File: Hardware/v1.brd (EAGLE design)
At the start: 50 x 40 mm, 82 parts, among them IC1 LM324D, IC2 m328p, IC3 REG1117, J1 22-27-2061-06, J2 22-27-2021-02, J3 22-27-2021-02, J4 22-27-2031-03, J5 22-27-2041-04, Q1 BSS123, Q2 BSS123, Q3 BSS123, Q5 BSS123

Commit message: solved all from #17
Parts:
- added R30: 1k, rcl:R0603
- moved TP4 5.48 mm to (27.4, 38.3), flipped to the bottom
- moved TP9 4.83 mm to (32.9, 38.4)
- moved TP10 4.65 mm to (33.3, 34.4)
- flipped TP6 to the top
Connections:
- new net N$27: C1.1, IC1.3, R30.2, TP4.TP
- net SENSOR0: now also R30.1; no longer C1.1, IC1.3, TP4.TP
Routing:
- net SENSOR0: track 63.8 -> 49.9 mm, vias 2 -> 1
- net N$27: track 0.00 -> 12.5 mm, vias 0 -> 1
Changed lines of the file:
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@@
 <?xml version="1.0" encoding="utf-8"?>
 <!DOCTYPE eagle SYSTEM "eagle.dtd">
-<eagle version="7.2.0">
+<eagle version="6.6.0">
 <drawing>
 <settings>
@@
 <layer number="32" name="bCream" color="7" fill="5" visible="no" active="yes"/>
 <layer number="33" name="tFinish" color="6" fill="3" visible="yes" active="yes"/>
-<layer number="34" name="bFinish" color="6" fill="6" visible="no" active="yes"/>
+<layer number="34" name="bFinish" color="6" fill="6" visible="yes" active="yes"/>
 <layer number="35" name="tGlue" color="7" fill="4" visible="no" active="yes"/>
 <layer number="36" name="bGlue" color="7" fill="5" visible="no" active="yes"/>
@@
 <text x="38.89375" y="39.0525" size="1.27" layer="33" font="vector" ratio="15" align="center">PD6</text>
 <text x="41.513125" y="33.9725" size="1.27" layer="33" font="vector" ratio="15" align="center">PD7</text>
-<text x="29.225875" y="37.7825" size="1.27" layer="33" font="vector" ratio="15" align="center">SENS0</text>
+<text x="31.670625" y="36.449" size="1.27" layer="34" font="vector" ratio="15" rot="MR0" align="center">SENS0</text>
 <text x="26.819225" y="9.877425" size="1.27" layer="33" font="vector" ratio="15" align="center">LK_0</text>
 <text x="14.6685" y="2.0955" size="1.27" layer="34" font="vector" ratio="15" rot="MR0" align="center">H</text>
@@
 <pass name="Default">
 <param name="RoutingGrid" value="3.125mil"/>
-<param name="AutoGrid" value="1"/>
-<param name="Efforts" value="0"/>
-<param name="TopRouterVariant" value="1"/>
 <param name="tpViaShape" value="round"/>
 <param name="PrefDir.1" value="|"/>
@@
 <attribute name="VALUE" x="30.11805" y="21.929725" size="0.0254" layer="28" rot="MR0"/>
 </element>
-<element name="TP4" library="testpad" package="B1,27" value="PTR1B1,27" x="32.8295" y="37.766625" smashed="yes">
-<attribute name="TP_SIGNAL_NAME" value="" x="32.1945" y="35.861625" size="1" layer="37"/>
-<attribute name="VALUE" x="32.1945" y="37.004625" size="0.0254" layer="27"/>
+<element name="TP4" library="testpad" package="B1,27" value="PTR1B1,27" x="27.3685" y="38.274625" smashed="yes" rot="MR0">
+<attribute name="TP_SIGNAL_NAME" value="" x="28.0035" y="36.369625" size="1" layer="38" rot="MR0"/>
+<attribute name="VALUE" x="28.0035" y="37.512625" size="0.0254" layer="28" rot="MR0"/>
 </element>
 <element name="TP5" library="testpad" package="B1,27" value="PTR1B1,27" x="28.622625" y="8.239125" smashed="yes">
@@
 <attribute name="NAME" x="34.3804" y="35.2791" size="1.143" layer="34" font="vector" ratio="15" rot="MR270"/>
 </element>
-<element name="TP6" library="testpad" package="B1,27" value="PTR1B1,27" x="2.159" y="25.908" smashed="yes" rot="MR0">
-<attribute name="TP_SIGNAL_NAME" value="" x="2.794" y="24.003" size="1" layer="38" rot="MR0"/>
-<attribute name="VALUE" x="2.794" y="25.146" size="0.0254" layer="28" rot="MR0"/>
+<element name="TP6" library="testpad" package="B1,27" value="PTR1B1,27" x="2.159" y="25.908" smashed="yes">
+<attribute name="TP_SIGNAL_NAME" value="" x="1.524" y="24.003" size="1" layer="37"/>
+<attribute name="VALUE" x="1.524" y="25.146" size="0.0254" layer="27"/>
 </element>
 <element name="TP8" library="testpad" package="B1,27" value="PTR1B1,27" x="9.0805" y="37.846" smashed="yes" rot="MR0">
@@
 <attribute name="VALUE" x="9.7155" y="37.084" size="0.0254" layer="28" rot="MR0"/>
 </element>
-<element name="TP9" library="testpad" package="B1,27" value="PTR1B1,27" x="28.067" y="38.227" smashed="yes" rot="MR0">
-<attribute name="TP_SIGNAL_NAME" value="" x="28.702" y="36.322" size="1" layer="38" rot="MR0"/>
-<attribute name="VALUE" x="28.702" y="37.465" size="0.0254" layer="28" rot="MR0"/>
-</element>
-<element name="TP10" library="testpad" package="B1,27" value="PTR1B1,27" x="30.6705" y="38.1635" smashed="yes" rot="MR0">
-<attribute name="TP_SIGNAL_NAME" value="" x="31.3055" y="36.2585" size="1" layer="38" rot="MR0"/>
-<attribute name="VALUE" x="31.3055" y="37.4015" size="0.0254" layer="28" rot="MR0"/>
+<element name="TP9" library="testpad" package="B1,27" value="PTR1B1,27" x="32.893" y="38.354" smashed="yes" rot="MR0">
+<attribute name="TP_SIGNAL_NAME" value="" x="33.528" y="36.449" size="1" layer="38" rot="MR0"/>
+<attribute name="VALUE" x="33.528" y="37.592" size="0.0254" layer="28" rot="MR0"/>
+</element>
+<element name="TP10" library="testpad" package="B1,27" value="PTR1B1,27" x="33.3375" y="34.3535" smashed="yes" rot="MR0">
+<attribute name="TP_SIGNAL_NAME" value="" x="33.9725" y="32.4485" size="1" layer="38" rot="MR0"/>
+<attribute name="VALUE" x="33.9725" y="33.5915" size="0.0254" layer="28" rot="MR0"/>
 </element>
 <element name="C9" library="rcl" package="E5-13" value="1000u" x="30.5435" y="12.0015" smashed="yes" rot="MR90">
@@
 <element name="R29" library="rcl" package="R0603" value="280" x="17.78" y="16.7005" smashed="yes">
 <attribute name="NAME" x="16.1925" y="14.859" size="1.143" layer="33" font="vector" ratio="15" rot="R90"/>
+</element>
+<element name="R30" library="rcl" package="R0603" value="1k" x="30.4165" y="36.3855" smashed="yes" rot="R180">
+<attribute name="NAME" x="31.9405" y="38.481" size="1.27" layer="33" font="vector" ratio="15" rot="R180"/>
 </element>
 </elements>
@@
 <via x="15.1765" y="31.6865" extent="1-16" drill="0.4"/>
 <via x="15.5321" y="25.746075" extent="1-16" drill="0.4"/>
-<via x="29.4386" y="37.239575" extent="1-16" drill="0.4"/>
+<via x="29.3751" y="39.144575" extent="1-16" drill="0.4"/>
 <via x="32.4231" y="39.271575" extent="1-16" drill="0.4"/>
 <via x="9.8171" y="36.731575" extent="1-16" drill="0.4"/>
@@
 </signal>
 <signal name="SENSOR0">
-<via x="32.8295" y="36.03625" extent="1-16" drill="0.6"/>
-<contactref element="IC1" pad="3"/>
-<contactref element="C1" pad="1"/>
-<contactref element="TP4" pad="TP"/>
-<wire x1="32.8295" y1="37.766625" x2="32.8295" y2="36.03625" width="1" layer="1"/>
-<wire x1="32.8295" y1="36.03625" x2="35.94735" y2="32.9184" width="1" layer="1"/>
+<wire x1="32.48025" y1="36.3855" x2="35.94735" y2="32.9184" width="1" layer="1"/>
 <wire x1="35.94735" y1="32.9184" x2="41.8084" y2="32.9184" width="1" layer="1"/>
 <wire x1="41.8084" y1="32.9184" x2="43.894375" y2="30.832425" width="1" layer="1"/>
@@
 <wire x1="40.513" y1="3.683" x2="39.76034375" y2="3.683" width="1" layer="16"/>
 <wire x1="39.76034375" y1="3.683" x2="38.263425" y2="5.179921875" width="1" layer="16"/>
-<wire x1="21.62175" y1="32.658375" x2="21.62175" y2="34.89325" width="1" layer="16"/>
-<wire x1="21.62175" y1="34.89325" x2="22.819625" y2="36.091125" width="1" layer="16"/>
-<wire x1="22.819625" y1="36.091125" x2="25.49525" y2="36.091125" width="1" layer="16"/>
-<wire x1="25.49525" y1="36.091125" x2="32.774625" y2="36.091125" width="1" layer="16"/>
-<wire x1="32.774625" y1="36.091125" x2="32.8295" y2="36.03625" width="1" layer="16"/>
+<contactref element="R30" pad="1"/>
+<wire x1="32.48025" y1="36.3855" x2="31.2665" y2="36.3855" width="1" layer="1"/>
 </signal>
 <signal name="ENABLE_LED_1">
@@
 <wire x1="19.905" y1="16.7005" x2="18.63" y2="16.7005" width="0.254" layer="1"/>
 </signal>
+<signal name="N$27">
+<contactref element="TP4" pad="TP"/>
+<contactref element="IC1" pad="3"/>
+<contactref element="C1" pad="1"/>
+<contactref element="R30" pad="2"/>
+<wire x1="29.5665" y1="36.3855" x2="27.3685" y2="36.3855" width="1" layer="1"/>
+<via x="27.3685" y="36.3855" extent="1-16" drill="0.6"/>
+<wire x1="27.3685" y1="36.3855" x2="27.074125" y2="36.091125" width="1" layer="16"/>
+<wire x1="27.074125" y1="36.091125" x2="25.49525" y2="36.091125" width="1" layer="16"/>
+<wire x1="25.49525" y1="36.091125" x2="23.137125" y2="36.091125" width="1" layer="16"/>
+<wire x1="23.137125" y1="36.091125" x2="21.62175" y2="34.57575" width="1" layer="16"/>
+<wire x1="21.62175" y1="34.57575" x2="21.62175" y2="32.658375" width="1" layer="16"/>
+<wire x1="27.3685" y1="36.3855" x2="27.3685" y2="38.274625" width="0.254" layer="16"/>
+</signal>
 </signals>

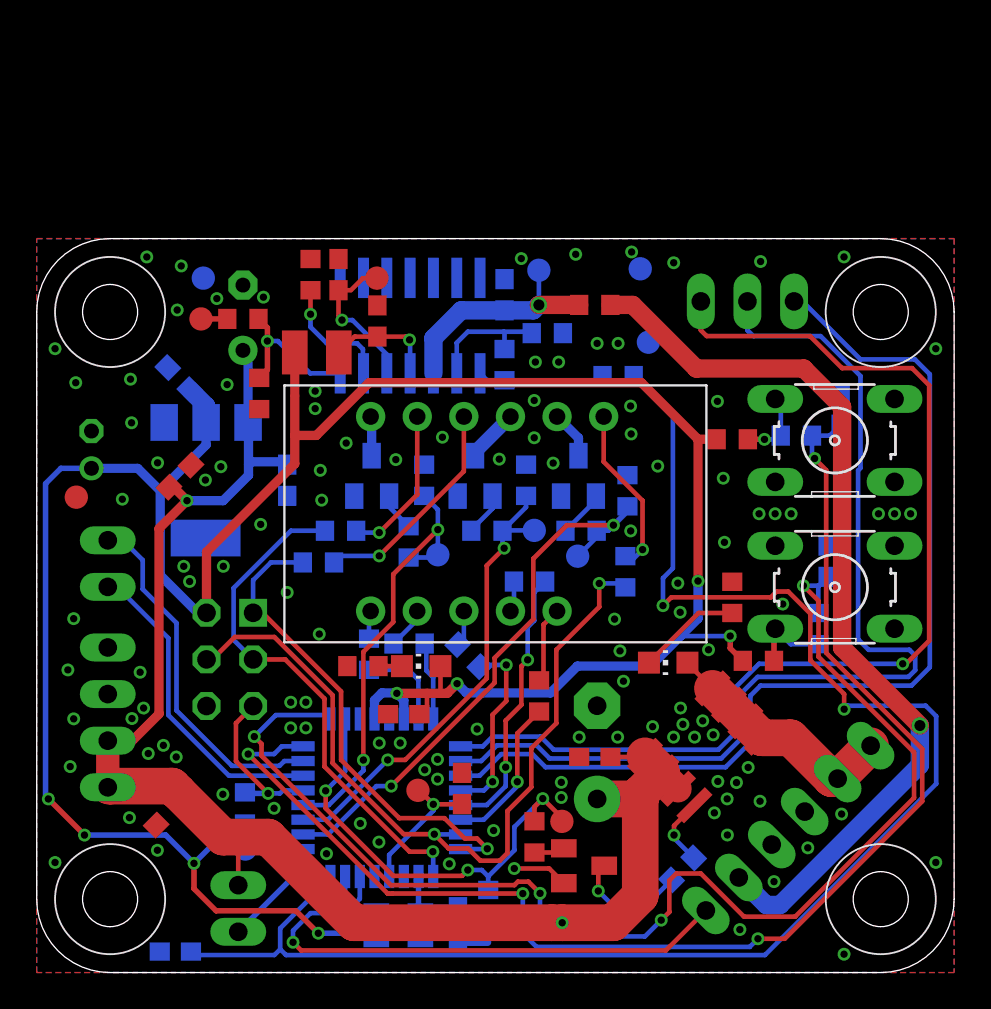
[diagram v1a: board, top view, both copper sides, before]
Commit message: Fixed issue #35 and added a third pin to make GND accessible when using UART.
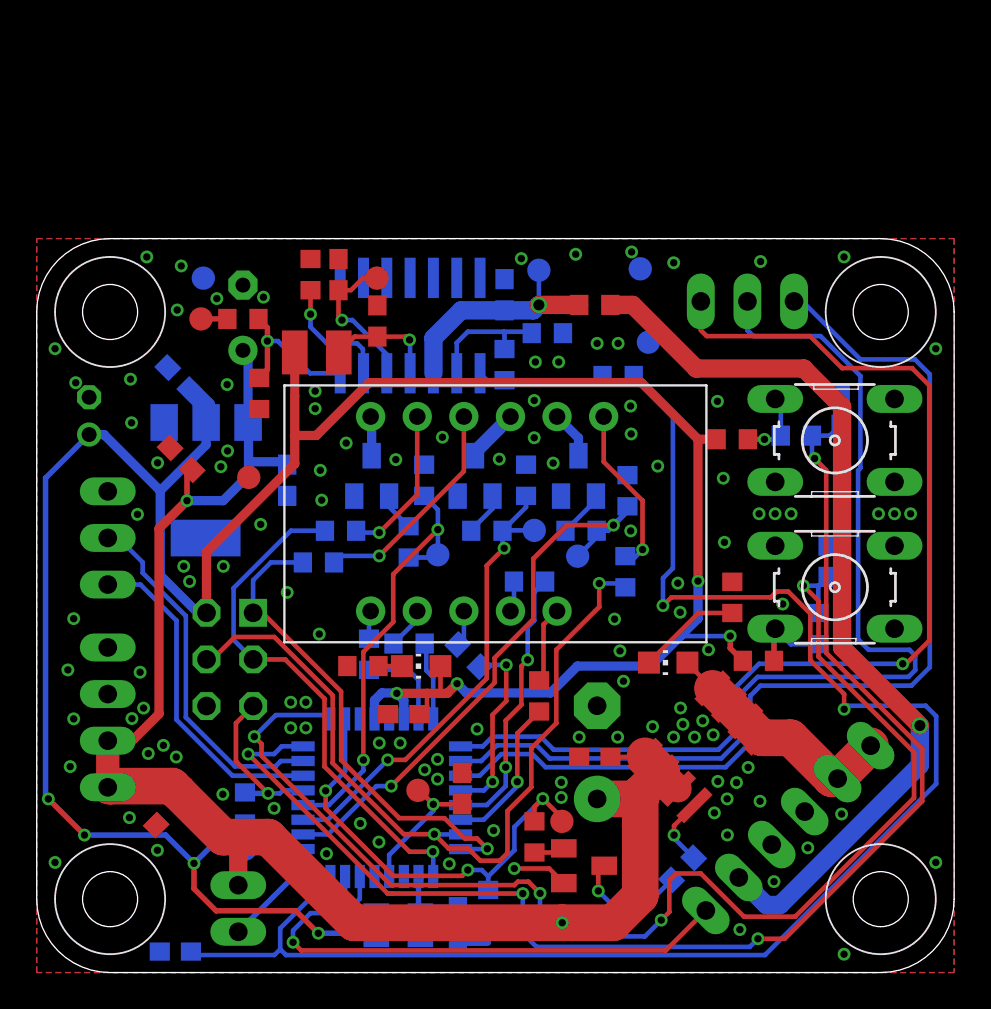
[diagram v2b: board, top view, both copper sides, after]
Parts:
- J2: value 22-27-2021-02 -> 22-27-2031-03; device con-molex:6410-02 -> con-molex:6410-03
- moved TP6 9.46 mm to (11.6, 27.0)
- moved C15 1.85 mm to (2.86, 30.3)
- moved J2 1.40 mm to (3.87, 23.7)
- moved C13 0.95 mm to (7.87, 28.0), turned to 315 degrees
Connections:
- net PD0 renamed N$29
- net PD1 renamed N$28
- net GND: now also J2.3
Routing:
- net VCC: track 146.8 -> 148.5 mm
- net N$29: track 17.4 -> 18.1 mm
- net 12V: track 84.7 -> 85.2 mm

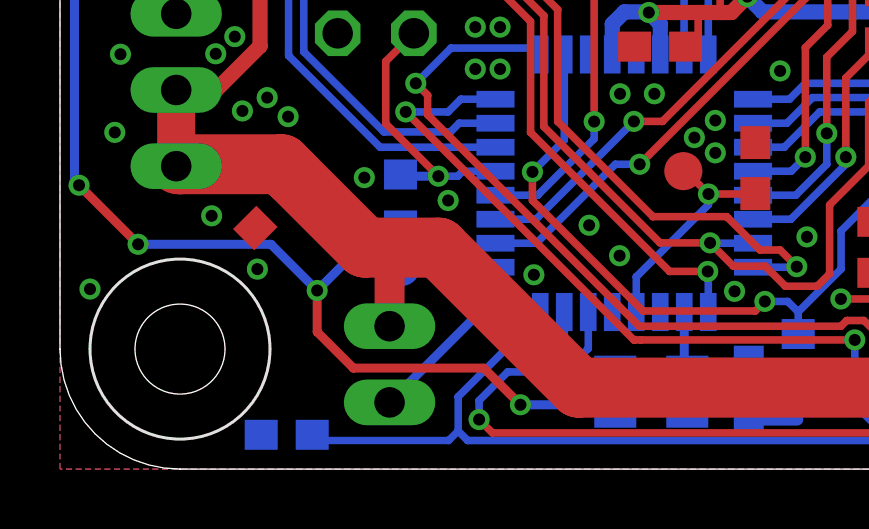
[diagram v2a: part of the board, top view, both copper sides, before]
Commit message: fixes issue #56
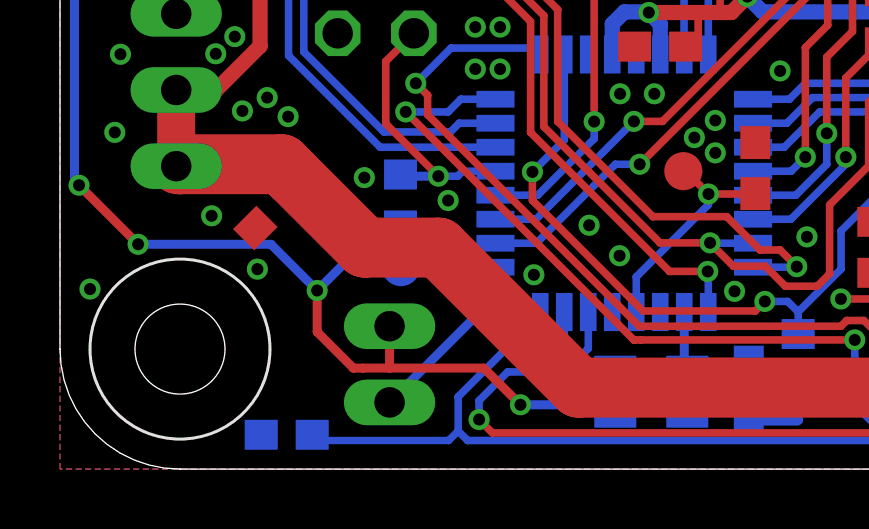
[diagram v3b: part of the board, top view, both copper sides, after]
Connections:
- net 12V: no longer J3.2
- net VCC: now also J3.2
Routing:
- net 12V: track 85.2 -> 83.4 mm
- net VCC: track 148.5 -> 149.9 mm
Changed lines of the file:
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@@
 <?xml version="1.0" encoding="utf-8"?>
 <!DOCTYPE eagle SYSTEM "eagle.dtd">
-<eagle version="6.6.0">
+<eagle version="7.2.0">
 <drawing>
 <settings>
@@
 <pass name="Default">
 <param name="RoutingGrid" value="3.125mil"/>
+<param name="AutoGrid" value="1"/>
+<param name="Efforts" value="0"/>
+<param name="TopRouterVariant" value="1"/>
 <param name="tpViaShape" value="round"/>
 <param name="PrefDir.1" value="|"/>
@@
 <wire x1="8.5725" y1="5.953125" x2="8.5725" y2="4.572" width="0.3" layer="1"/>
 <wire x1="8.5725" y1="4.572" x2="9.779" y2="3.3655" width="0.3" layer="1"/>
-<wire x1="9.779" y1="3.3655" x2="14.125575" y2="3.3655" width="0.3" layer="1"/>
+<wire x1="9.779" y1="3.3655" x2="10.0965" y2="3.3655" width="0.3" layer="1"/>
+<wire x1="10.9855" y1="3.3655" x2="14.125575" y2="3.3655" width="0.3" layer="1"/>
 <wire x1="9.2329" y1="28.75915" x2="6.731" y2="26.25725" width="0.508" layer="16"/>
 <wire x1="6.731" y1="26.25725" x2="6.731" y2="21.6535" width="0.508" layer="16"/>
@@
 <wire x1="3.667125" y1="29.321125" x2="2.8575" y2="29.321125" width="0.508" layer="16"/>
 <wire x1="0.4826" y1="26.946225" x2="2.8575" y2="29.321125" width="0.3" layer="16"/>
+<contactref element="J3" pad="2"/>
+<wire x1="10.0965" y1="3.3655" x2="10.9855" y2="3.3655" width="0.3" layer="1"/>
+<wire x1="10.9855" y1="3.3655" x2="10.9855" y2="4.7625" width="0.3" layer="1"/>
 </signal>
 <signal name="GND">
@@
 <wire x1="11.5189" y1="29.97835" x2="11.5189" y2="33.6296" width="0.5" layer="16"/>
 <wire x1="11.5189" y1="33.6296" x2="11.2395" y2="33.909" width="0.5" layer="16"/>
-<contactref element="J3" pad="2"/>
 <wire x1="10.16" y1="7.381875" x2="10.9855" y2="6.556375" width="0.254" layer="1"/>
-<wire x1="10.9855" y1="6.556375" x2="10.9855" y2="4.7625" width="1" layer="1"/>
 <wire x1="31.2665" y1="11.7475" x2="33.088171875" y2="11.7475" width="0.254" layer="1"/>
 <wire x1="33.088171875" y1="11.7475" x2="33.15235625" y2="11.811684375" width="0.254" layer="1"/>

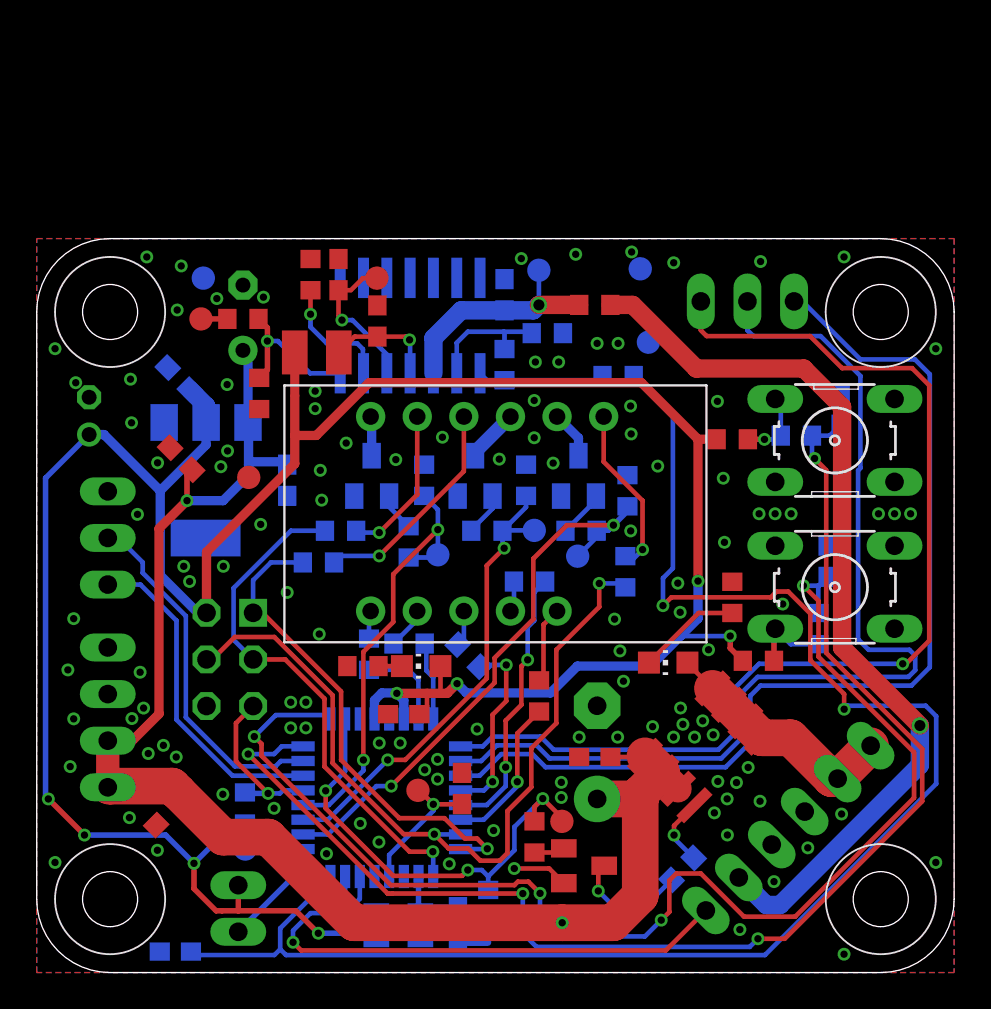
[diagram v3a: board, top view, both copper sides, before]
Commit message: - changed the 6pin header to a 7pin header to deliver 5V as well on one pin (see #60) - reduced sensor wire from 1mm to 0.8mm - rearrange wiring to compensate changes
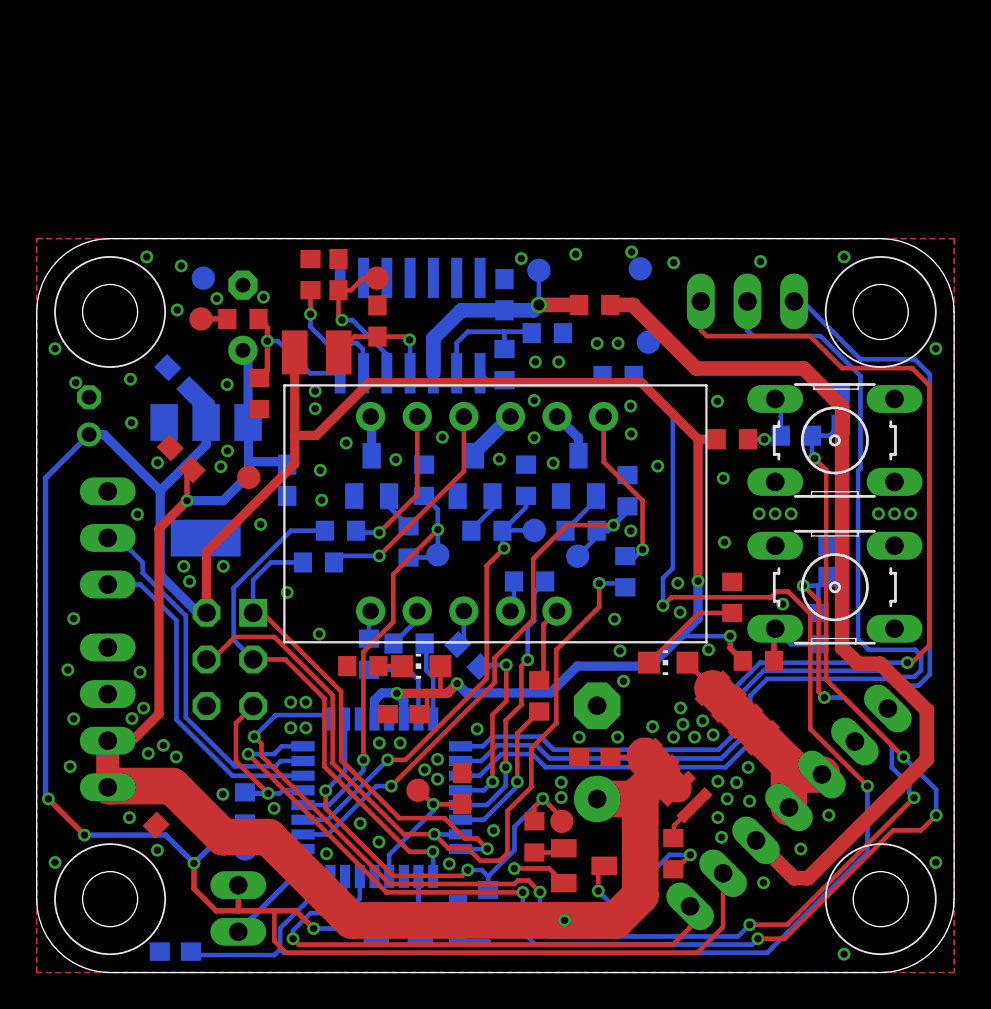
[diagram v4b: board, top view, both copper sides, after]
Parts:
- removed J1: 22-27-2061-06, con-molex:6410-06
- added J6: 22-27-2071-07, con-molex:6410-07
- moved R15 0.97 mm to (34.7, 6.48), flipped to the top, turned to 270 degrees
- moved C5 0.13 mm to (23.0, 2.84)
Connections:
- removed net ADC7: IC2.22, J1.1
- new net STH: IC2.24, J3.1
- net GND: now also J6.6, J6.7; no longer J1.3, J1.4
- net HALL: now also IC2.22, J6.1; no longer IC2.24, J3.1
- net N$33: now also J6.4, J6.5; no longer J1.5, J1.6
- net SENSOR0: now also J6.3; no longer J1.2
- net VCC: now also J6.2
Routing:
- net ADC7: track 29.8 -> 0.00 mm, vias 1 -> 0
- net VCC: track 149.9 -> 179.5 mm
- net HALL: track 6.27 -> 29.3 mm, vias 0 -> 1
- net STH: track 0.00 -> 6.27 mm
- net THERMO0: track 88.7 -> 82.6 mm
- net N$32: track 6.98 -> 10.7 mm, vias 1 -> 2
- net BUTTON_-: track 70.0 -> 67.7 mm, vias 4 -> 6
- net N$15: track 3.77 -> 2.27 mm, vias 1 -> 0
- net BUTTON_+: track 73.0 -> 74.5 mm, vias 4 -> 6
- net N$33: track 13.4 -> 12.2 mm
- net PD6: track 56.3 -> 57.2 mm
- net PD7: track 55.1 -> 55.6 mm
- net SENSOR0: track 49.9 -> 49.6 mm, vias 1 -> 0
- net GND: track 4.74 -> 4.83 mm, vias 117 -> 116
